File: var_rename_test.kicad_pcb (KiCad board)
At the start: 2 copper layers, 1 part

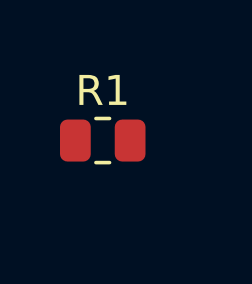
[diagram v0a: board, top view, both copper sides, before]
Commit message: trying with footprint in user lib
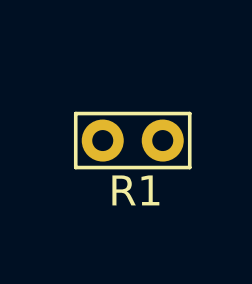
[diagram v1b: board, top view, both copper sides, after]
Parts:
- R1: footprint Resistor_SMD:R_0805_2012Metric -> var_rename:TestPoint_Bridge_Pitch2.0mm_Drill0.7mm
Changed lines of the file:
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@@
 	(net 0 "")
 	(net 1 "unconnected-(R1-Pad1)")
-	(net 2 "unconnected-(R1-Pad2)")
-	(footprint "Resistor_SMD:R_0805_2012Metric"
+	(footprint "var_rename:TestPoint_Bridge_Pitch2.0mm_Drill0.7mm"
 		(layer "F.Cu")
 		(at 136.2475 82.804)
-		(descr "Resistor SMD 0805 (2012 Metric), square (rectangular) end terminal, IPC_7351 nominal, (Body size source: IPC-SM-782 page 72, https://www.pcb-3d.com/wordpress/wp-content/uploads/ipc-sm-782a_amendment_1_and_2.pdf), generated with kicad-footprint-generator")
-		(tags "resistor")
+		(descr "wire loop as test point, pitch 2.0mm, hole diameter 0.7mm, wire diameter 0.5mm")
+		(tags "test point wire loop")
 		(property "Reference" "R1"
-			(at 0 -1.65 0)
+			(at 1.1 1.7 0)
 			(layer "F.SilkS")
 			(effects
@@
 		)
 		(property "Value" "R"
-			(at 0 1.65 0)
-			(layer "F.Fab")
-			(effects
-				(font
-					(size 1 1)
-					(thickness 0.15)
-				)
-			)
-		)
-		(property "Footprint" "Resistor_SMD:R_0805_2012Metric"
+			(at 1 -1.7 0)
+			(layer "F.Fab")
+			(effects
+				(font
+					(size 1 1)
+					(thickness 0.15)
+				)
+			)
+		)
+		(property "Footprint" "var_rename:TestPoint_Bridge_Pitch2.0mm_Drill0.7mm"
 			(at 0 0 0)
 			(unlocked yes)
@@
 			)
 		)
-		(property "left:Footprint" "Resistor_SMD:R_0805_2012Metric"
-			(at 0 0 0)
-			(unlocked yes)
-			(layer "F.Fab")
-			(hide yes)
-			(effects
-				(font
-					(size 1 1)
-					(thickness 0.15)
-				)
-			)
-		)
-		(property "right:Footprint" "TestPoint:TestPoint_Bridge_Pitch2.0mm_Drill0.7mm"
+		(property "left:Footprint" "var_rename:D_0805_2012Metric"
+			(at 0 0 0)
+			(unlocked yes)
+			(layer "F.Fab")
+			(hide yes)
+			(effects
+				(font
+					(size 1 1)
+					(thickness 0.15)
+				)
+			)
+		)
+		(property "right:Footprint" "var_rename:TestPoint_Bridge_Pitch2.0mm_Drill0.7mm"
 			(at 0 0 0)
 			(unlocked yes)
@@
 		(sheetname "Root")
 		(sheetfile "var_rename_test.kicad_sch")
-		(attr smd)
-		(fp_line
-			(start -0.227064 -0.735)
-			(end 0.227064 -0.735)
-			(stroke
-				(width 0.12)
-				(type solid)
-			)
-			(layer "F.SilkS")
-		)
-		(fp_line
-			(start -0.227064 0.735)
-			(end 0.227064 0.735)
-			(stroke
-				(width 0.12)
-				(type solid)
-			)
-			(layer "F.SilkS")
-		)
-		(fp_line
-			(start -1.68 -0.95)
-			(end 1.68 -0.95)
-			(stroke
-				(width 0.05)
-				(type solid)
-			)
-			(layer "F.CrtYd")
-		)
-		(fp_line
-			(start -1.68 0.95)
-			(end -1.68 -0.95)
-			(stroke
-				(width 0.05)
-				(type solid)
-			)
-			(layer "F.CrtYd")
-		)
-		(fp_line
-			(start 1.68 -0.95)
-			(end 1.68 0.95)
-			(stroke
-				(width 0.05)
-				(type solid)
-			)
-			(layer "F.CrtYd")
-		)
-		(fp_line
-			(start 1.68 0.95)
-			(end -1.68 0.95)
-			(stroke
-				(width 0.05)
-				(type solid)
-			)
-			(layer "F.CrtYd")
-		)
-		(fp_line
-			(start -1 -0.625)
-			(end 1 -0.625)
-			(stroke
-				(width 0.1)
-				(type solid)
-			)
-			(layer "F.Fab")
-		)
-		(fp_line
-			(start -1 0.625)
-			(end -1 -0.625)
-			(stroke
-				(width 0.1)
-				(type solid)
-			)
-			(layer "F.Fab")
-		)
-		(fp_line
-			(start 1 -0.625)
-			(end 1 0.625)
-			(stroke
-				(width 0.1)
-				(type solid)
-			)
-			(layer "F.Fab")
-		)
-		(fp_line
-			(start 1 0.625)
-			(end -1 0.625)
-			(stroke
-				(width 0.1)
+		(attr through_hole)
+		(fp_line
+			(start -0.9 -0.9)
+			(end -0.9 0.9)
+			(stroke
+				(width 0.12)
+				(type solid)
+			)
+			(layer "F.SilkS")
+		)
+		(fp_line
+			(start -0.9 0.9)
+			(end 2.9 0.9)
+			(stroke
+				(width 0.12)
+				(type solid)
+			)
+			(layer "F.SilkS")
+		)
+		(fp_line
+			(start 2.9 -0.9)
+			(end -0.9 -0.9)
+			(stroke
+				(width 0.12)
+				(type solid)
+			)
+			(layer "F.SilkS")
+		)
+		(fp_line
+			(start 2.9 0.9)
+			(end 2.9 -0.9)
+			(stroke
+				(width 0.12)
+				(type solid)
+			)
+			(layer "F.SilkS")
+		)
+		(fp_line
+			(start -1.2 1.2)
+			(end -1.2 -1.2)
+			(stroke
+				(width 0.05)
+				(type solid)
+			)
+			(layer "F.CrtYd")
+		)
+		(fp_line
+			(start -1.2 1.2)
+			(end 3.2 1.2)
+			(stroke
+				(width 0.05)
+				(type solid)
+			)
+			(layer "F.CrtYd")
+		)
+		(fp_line
+			(start 3.2 -1.2)
+			(end -1.2 -1.2)
+			(stroke
+				(width 0.05)
+				(type solid)
+			)
+			(layer "F.CrtYd")
+		)
+		(fp_line
+			(start 3.2 -1.2)
+			(end 3.2 1.2)
+			(stroke
+				(width 0.05)
+				(type solid)
+			)
+			(layer "F.CrtYd")
+		)
+		(fp_line
+			(start 2 0)
+			(end 0 0)
+			(stroke
+				(width 0.12)
 				(type solid)
 			)
@@
 		)
 		(fp_text user "${REFERENCE}"
-			(at 0 0 0)
-			(layer "F.Fab")
-			(effects
-				(font
-					(size 0.5 0.5)
-					(thickness 0.08)
-				)
-			)
-		)
-		(pad "1" smd roundrect
-			(at -0.9125 0)
-			(size 1.025 1.4)
-			(layers "F.Cu" "F.Paste" "F.Mask")
-			(roundrect_rratio 0.243902)
+			(at 1.1 1.7 0)
+			(layer "F.Fab")
+			(effects
+				(font
+					(size 1 1)
+					(thickness 0.15)
+				)
+			)
+		)
+		(pad "1" thru_hole circle
+			(at 0 0)
+			(size 1.4 1.4)
+			(drill 0.7)
+			(layers "*.Cu" "*.Mask")
+			(remove_unused_layers no)
 			(net 1 "unconnected-(R1-Pad1)")
 			(pintype "passive")
 		)
-		(pad "2" smd roundrect
-			(at 0.9125 0)
-			(size 1.025 1.4)
-			(layers "F.Cu" "F.Paste" "F.Mask")
-			(roundrect_rratio 0.243902)
-			(net 2 "unconnected-(R1-Pad2)")
+		(pad "1" thru_hole circle
+			(at 2 0)
+			(size 1.4 1.4)
+			(drill 0.7)
+			(layers "*.Cu" "*.Mask")
+			(remove_unused_layers no)
+			(net 1 "unconnected-(R1-Pad1)")
 			(pintype "passive")
 		)
-		(model "${KICAD8_3DMODEL_DIR}/Resistor_SMD.3dshapes/R_0805_2012Metric.wrl"
+		(model "${KICAD8_3DMODEL_DIR}/TestPoint.3dshapes/TestPoint_Bridge_Pitch2.0mm_Drill0.7mm.wrl"
 			(offset
 				(xyz 0 0 0)
